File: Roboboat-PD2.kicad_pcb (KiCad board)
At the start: 2 copper layers, 78 x 60.7 mm, 52 parts, among them J1 14.4V, J10 Motor, J11 Motor, J12 Motor, J13 Motor, J14 Motor, J15 Motor, J16 Motor, J17 GND TP, J18 PGOOD TP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

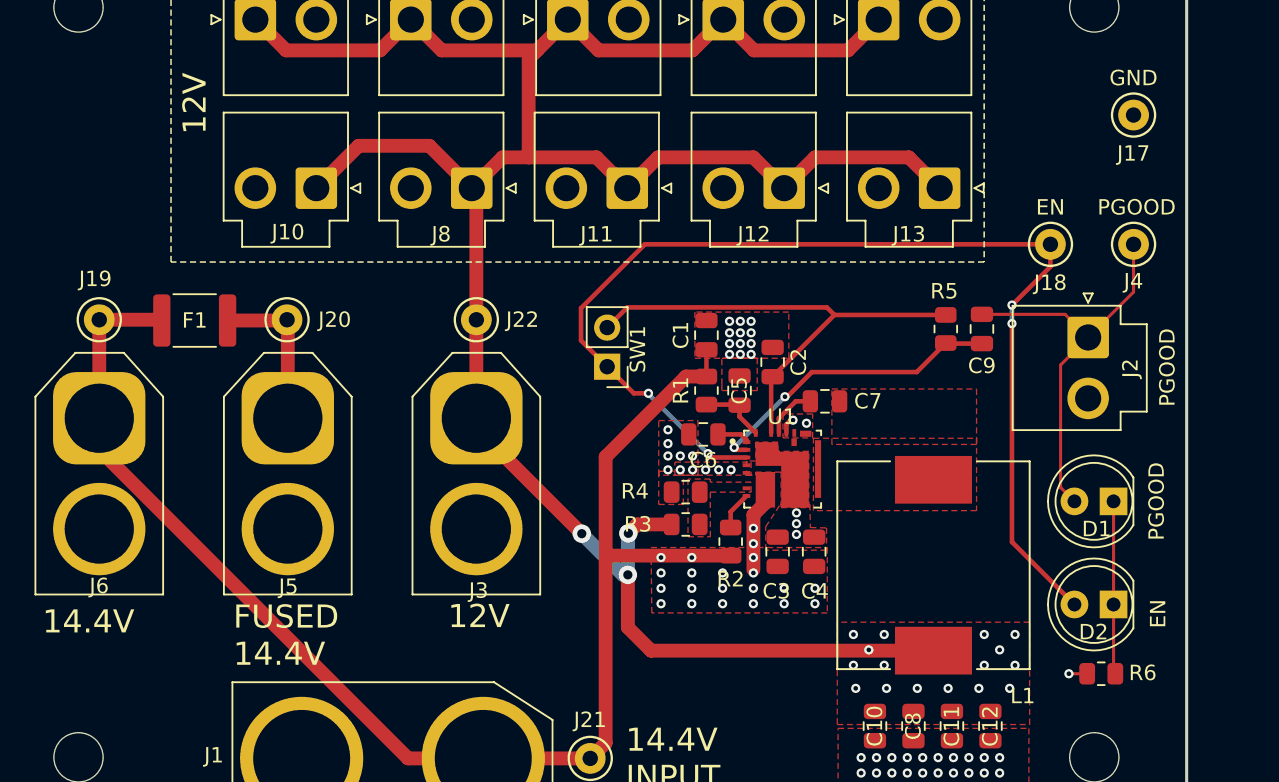
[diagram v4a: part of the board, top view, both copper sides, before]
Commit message: give each LED its own resistor
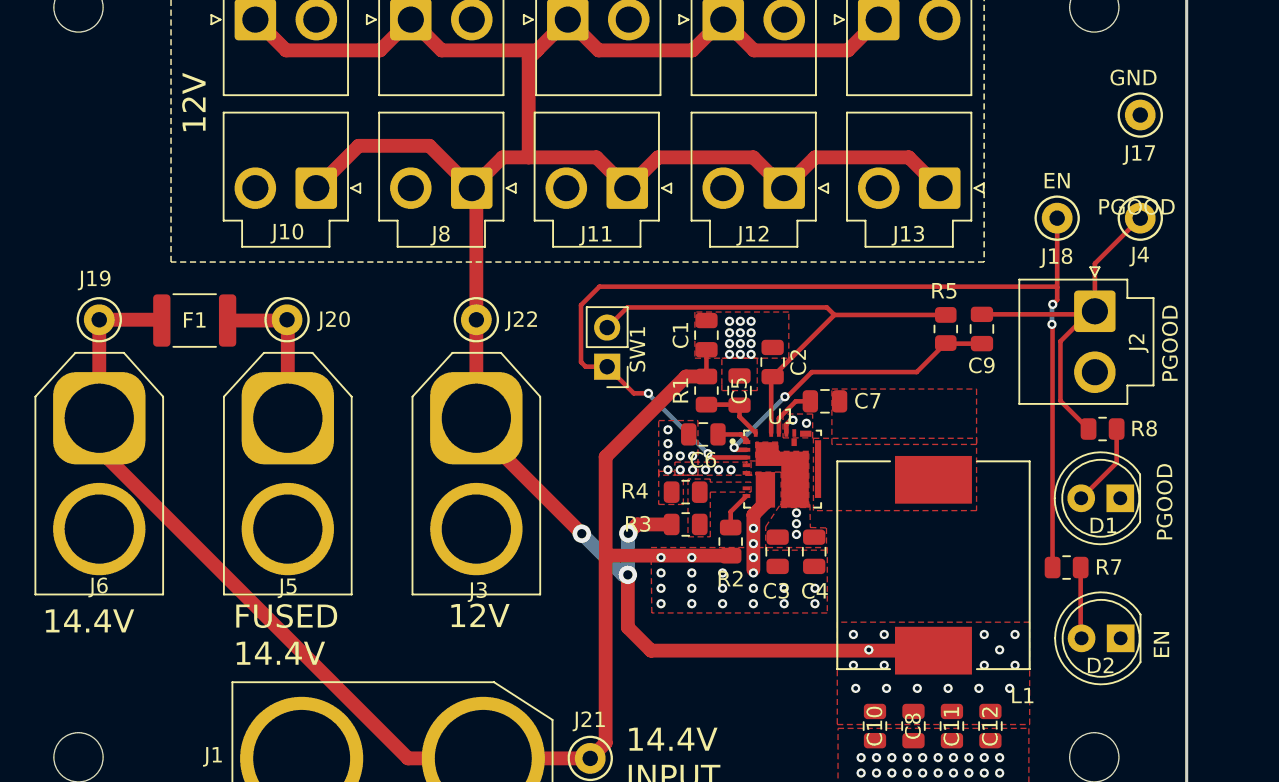
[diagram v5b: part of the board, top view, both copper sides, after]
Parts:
- removed R6: 220, Resistor_SMD:R_0805_2012Metric
- added R7: 220, Resistor_SMD:R_0805_2012Metric, F.Cu at (164.8, 110.7)
- added R8: 220, Resistor_SMD:R_0805_2012Metric, F.Cu at (167.2, 101.7)
- C10, C11, C12, C8: value 88uF -> 22uF
- D2: value GREEN -> BLUE LED
- R2: value 960 -> 960k
- moved D2 2.25 mm to (168.4, 115.2)
- moved J18 1.76 mm to (164.2, 88.0)
- moved J2 1.76 mm to (166.7, 94.0)
- moved J4 1.76 mm to (169.6, 88.0)
- moved D1 0.48 mm to (168.3, 106.2)
- moved J17 0.44 mm to (169.6, 81.2)
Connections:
- D1 pad 1: Net-(D1-K) -> GND
- D1 pad 2: /PGOOD -> Net-(D1-A)
- D2 pad 1: Net-(D1-K) -> GND
- D2 pad 2: /EN -> Net-(D2-A)
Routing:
- net Net-(D1-K): track 11.1 -> 0.00 mm
- net Net-(D1-A): track 0.00 -> 5.45 mm
- net Net-(D2-A): track 0.00 -> 4.62 mm
- net /EN: track 74.4 -> 71.4 mm
- net /PGOOD: track 26.6 -> 24.2 mm
- net +14.4V: track 96.6 -> 94.5 mm
- net GND: track 2.29 -> 1.10 mm, vias 59 -> 58

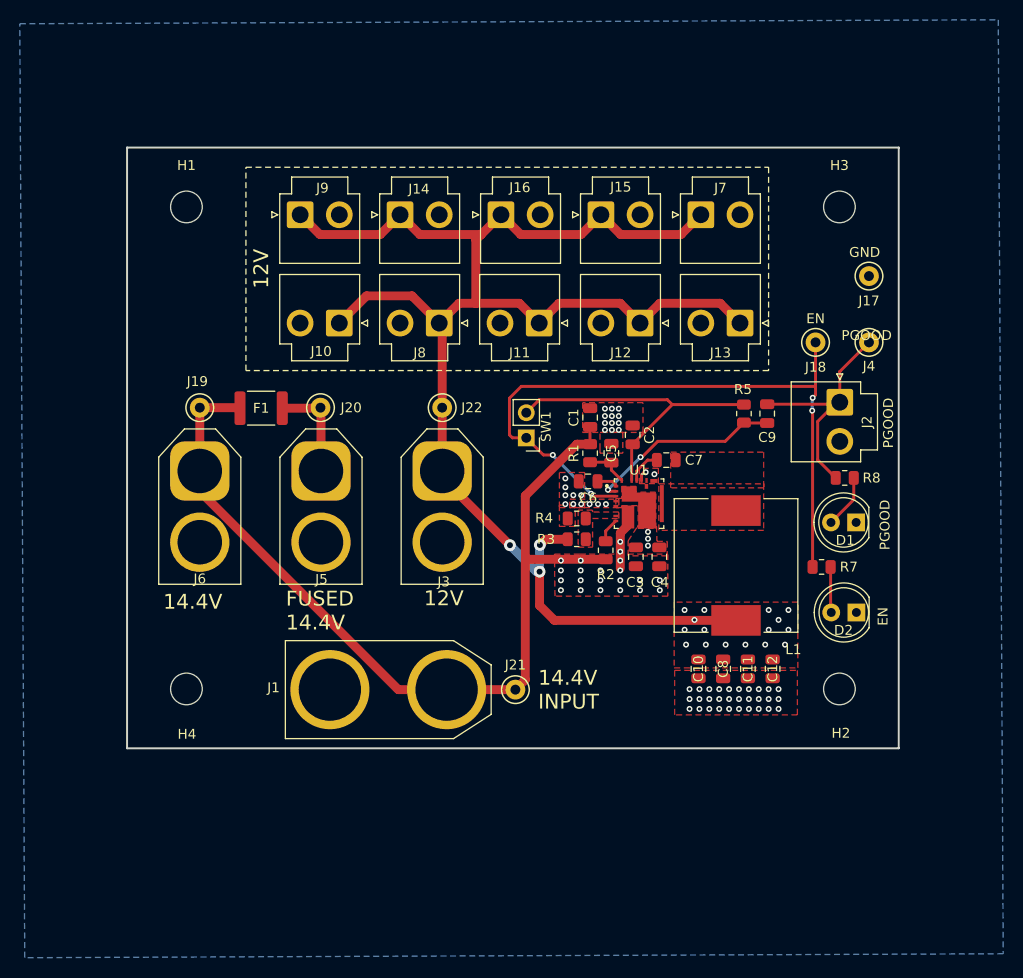
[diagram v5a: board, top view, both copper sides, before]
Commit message: use test point symbol, wire PFM to VCC
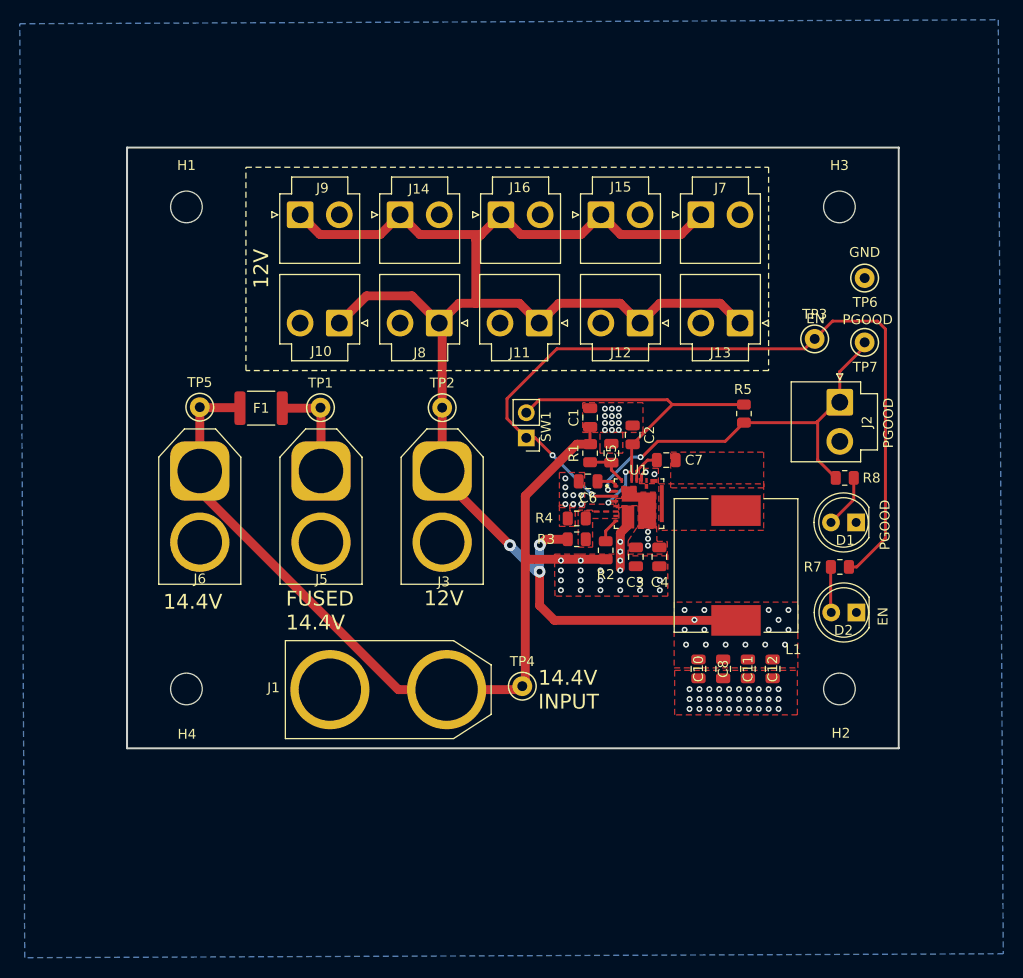
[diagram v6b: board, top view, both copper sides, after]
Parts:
- removed C9: 0.1uF, Capacitor_SMD:C_0805_2012Metric
- removed J17: GND TP, TestPoint:TestPoint_Keystone_5000-5004_Miniature
- removed J18, J19, J20, J21, J22, J4: PGOOD TP, TestPoint:TestPoint_Keystone_5000-5004_Miniature
- added TP1: TestPoint, TestPoint:TestPoint_Keystone_5000-5004_Miniature, F.Cu at (114.2, 94.5)
- added TP2: TestPoint, TestPoint:TestPoint_Keystone_5000-5004_Miniature, F.Cu at (126.5, 94.5)
- added TP3: TestPoint, TestPoint:TestPoint_Keystone_5000-5004_Miniature, F.Cu at (164.2, 87.6)
- added TP4: TestPoint, TestPoint:TestPoint_Keystone_5000-5004_Miniature, F.Cu at (134.6, 122.7)
- added TP5: TestPoint, TestPoint:TestPoint_Keystone_5000-5004_Miniature, F.Cu at (102.0, 94.5)
- added TP6: TestPoint, TestPoint:TestPoint_Keystone_5000-5004_Miniature, F.Cu at (169.2, 81.5)
- added TP7: TestPoint, TestPoint:TestPoint_Keystone_5000-5004_Miniature, F.Cu at (169.2, 88.0)
- R1: value 100k -> 1.5
- moved R7 1.85 mm to (166.7, 110.7), turned to 0 degrees
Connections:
- net /14.4_F renamed Net-(J5-Pin_1)
- R5 pad 2: Net-(U1-PGOOD) -> /PGOOD
- U1 pad 2: Net-(U1-PGOOD) -> /PGOOD
- U1 pad 4: GND -> /VCC
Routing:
- net Net-(U1-PGOOD): track 19.7 -> 0.00 mm, vias 2 -> 0
- net /PGOOD: track 24.2 -> 41.9 mm, vias 0 -> 2
- net /EN: track 71.4 -> 84.1 mm, vias 4 -> 2
- net /VCC: track 32.0 -> 37.2 mm, vias 0 -> 2
- net GND: vias 58 -> 55

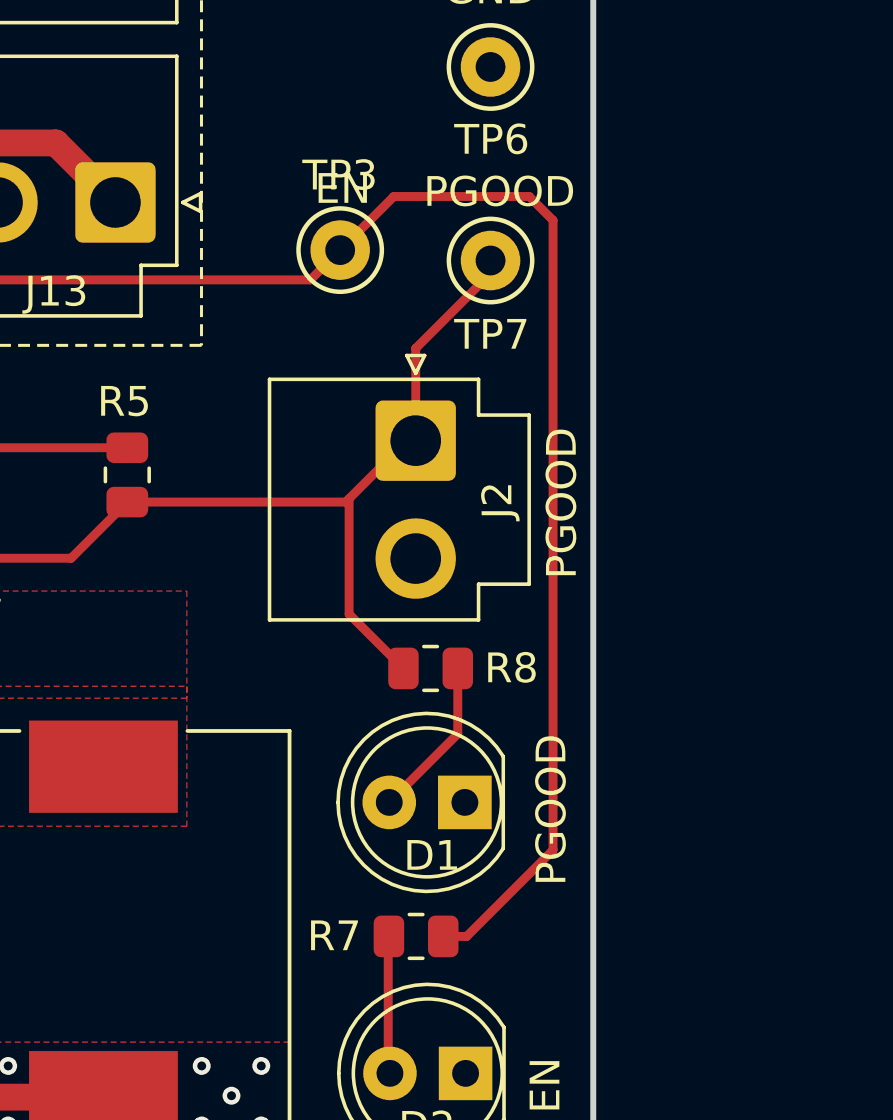
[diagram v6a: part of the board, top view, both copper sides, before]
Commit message: move PGOOD test point
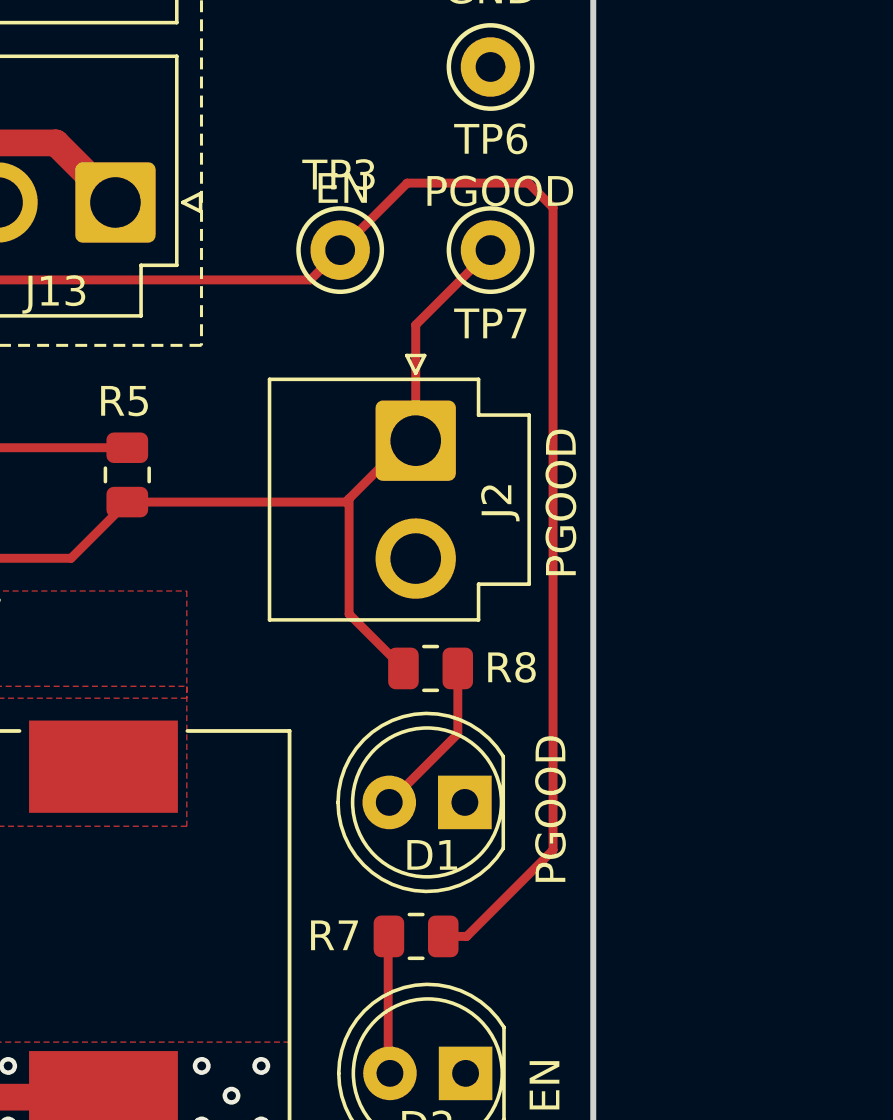
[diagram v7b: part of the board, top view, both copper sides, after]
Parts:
- moved TP7 0.35 mm to (169.2, 87.6)
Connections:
- U1 pad 2: /PGOOD -> unconnected-(U1-PGOOD-Pad2)
- U1 pad 24: unconnected-(U1-NC-Pad24) -> Net-(U1-AIN)
- U1 pad 28: Net-(U1-AIN) -> (no net)
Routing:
- net /EN: track 84.1 -> 84.7 mm

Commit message: fix AOZ2379QI symbol
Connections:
- U1 pad 2: unconnected-(U1-PGOOD-Pad2) -> /PGOOD
- U1 pad 24: Net-(U1-AIN) -> unconnected-(U1-NC-Pad24)
- U1 pad 28: (no net) -> Net-(U1-AIN)
- U1 pad 29: (no net) -> unconnected-(U1-NC-Pad29)
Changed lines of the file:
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@@
 	(net 14 "Net-(J5-Pin_1)")
 	(net 15 "Net-(U1-TON)")
-	(net 16 "unconnected-(U1-PGOOD-Pad2)")
+	(net 16 "unconnected-(U1-NC-Pad24)")
+	(net 17 "unconnected-(U1-NC-Pad29)")
 	(footprint "TestPoint:TestPoint_Keystone_5000-5004_Miniature"
 		(layer "F.Cu")
@@
 		(tags "resistor")
 		(property "Reference" "R8"
-			(at -2.7125 0 360)
+			(at -2.7125 0 0)
 			(layer "F.SilkS")
 			(effects
@@
 		)
 		(property "Value" "220"
-			(at 0 1.65 360)
+			(at 0 1.65 0)
 			(layer "F.Fab")
 			(effects
@@
 		)
 		(fp_text user "${REFERENCE}"
-			(at 0 0 360)
+			(at 0 0 0)
 			(layer "F.Fab")
 			(effects
@@
 			(size 0.5 0.25)
 			(layers "F.Cu" "F.Paste" "F.Mask")
-			(net 16 "unconnected-(U1-PGOOD-Pad2)")
+			(net 10 "/PGOOD")
 			(pinfunction "PGOOD")
 			(pintype "input")
@@
 			(size 0.25 0.5)
 			(layers "F.Cu" "F.Paste" "F.Mask")
-			(net 2 "Net-(U1-AIN)")
-			(pinfunction "AIN")
-			(pintype "input")
+			(net 16 "unconnected-(U1-NC-Pad24)")
+			(pinfunction "NC")
+			(pintype "no_connect")
 			(solder_mask_margin 0.102)
 		)
@@
 			(size 0.25 0.5)
 			(layers "F.Cu" "F.Paste" "F.Mask")
+			(net 2 "Net-(U1-AIN)")
+			(pinfunction "AIN")
+			(pintype "input")
 			(solder_mask_margin 0.102)
 		)
@@
 			(size 0.35 0.5)
 			(layers "F.Cu" "F.Paste" "F.Mask")
+			(net 17 "unconnected-(U1-NC-Pad29)")
+			(pinfunction "NC")
+			(pintype "no_connect")
 			(solder_mask_margin 0.102)
 		)
@@
 		(tags "resistor")
 		(property "Reference" "R7"
-			(at -2.75 0 360)
+			(at -2.75 0 0)
 			(layer "F.SilkS")
 			(effects
@@
 		)
 		(property "Value" "220"
-			(at 0 1.65 360)
+			(at 0 1.65 0)
 			(layer "F.Fab")
 			(effects
@@
 		)
 		(fp_text user "${REFERENCE}"
-			(at 0 0 360)
+			(at 0 0 0)
 			(layer "F.Fab")
 			(effects
@@
 	)
 	(segment
-		(start 143.6 100.1)
-		(end 143.6 100.85)
+		(start 141.45 100.0625)
+		(end 143.5625 100.0625)
 		(width 0.3)
 		(layer "F.Cu")
@@
 	)
 	(segment
-		(start 141.45 100.0625)
-		(end 143.5625 100.0625)
+		(start 143.6 100.1)
+		(end 143.6 100.85)
 		(width 0.3)
 		(layer "F.Cu")
